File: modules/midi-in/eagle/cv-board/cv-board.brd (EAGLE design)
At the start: 100 x 80 mm, 50 parts, among them IC2 TL072P, IC3 TL074P, IC4 TL074P, T1 BC547, T2 BC547, X1 POWER IN

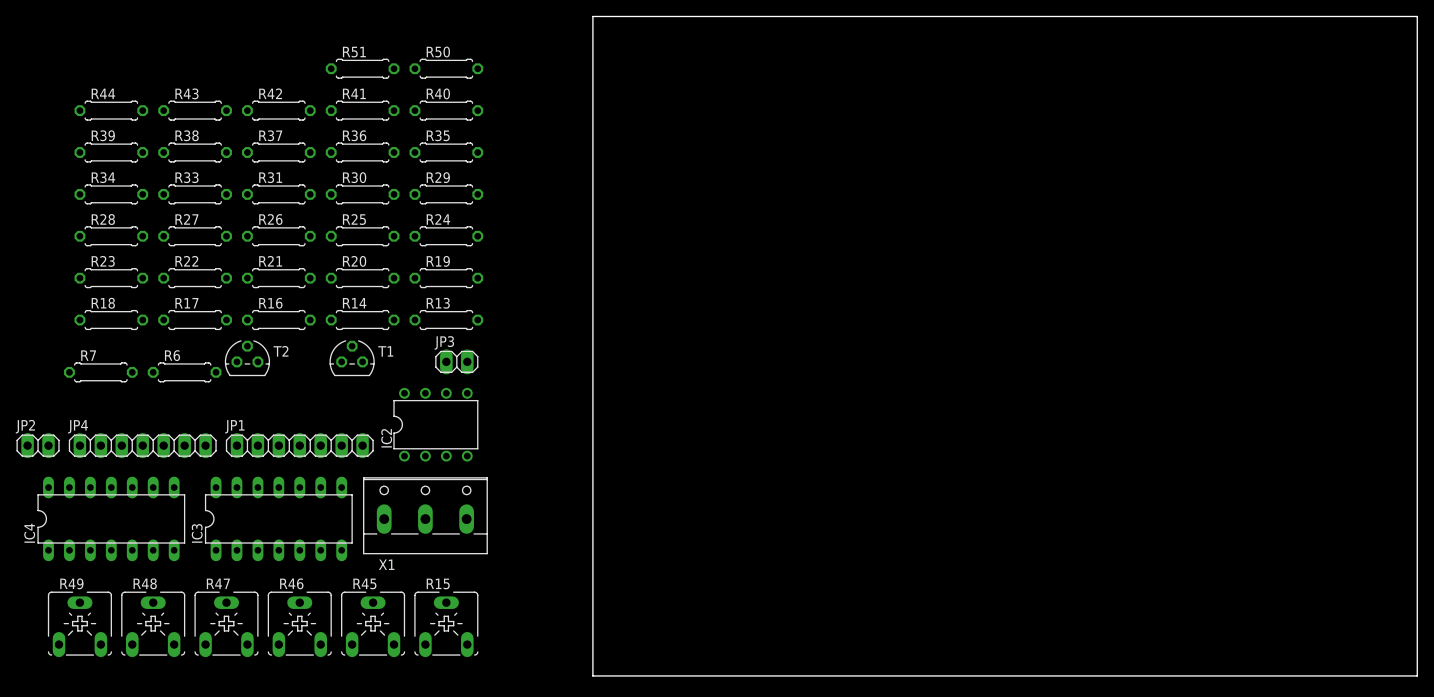
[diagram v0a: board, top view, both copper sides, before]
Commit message: Probably doomed attempt at routing CV board.
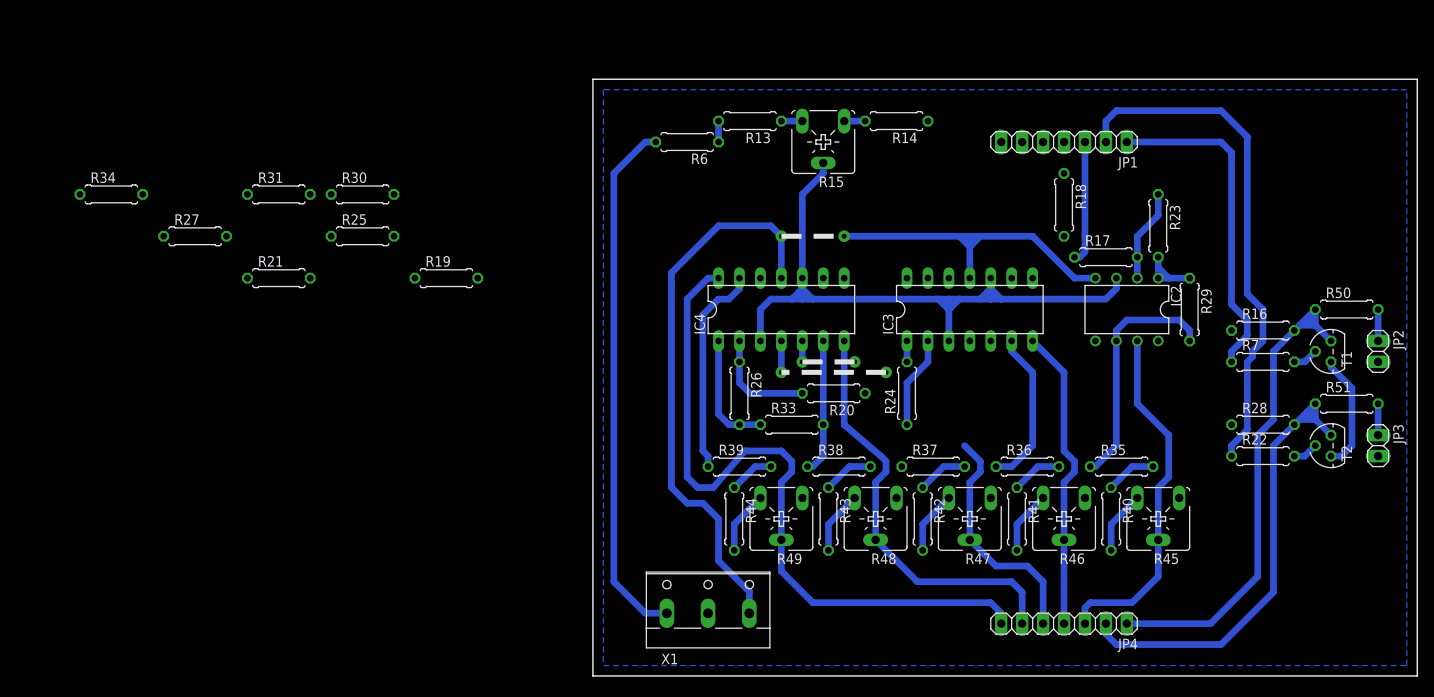
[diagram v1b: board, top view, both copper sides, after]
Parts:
- moved JP2 163.0 mm to (95.2, 39.4), turned to 270 degrees
- moved R28 141.6 mm to (81.3, 30.5)
- moved R7 141.0 mm to (81.3, 38.1)
- moved T2 131.8 mm to (89.5, 27.9), turned to 90 degrees
- moved R22 131.3 mm to (81.3, 26.7)
- moved R23 127.2 mm to (68.6, 54.6), turned to 270 degrees
- moved R51 126.1 mm to (91.4, 33.0)
- moved R16 119.4 mm to (81.3, 41.9)
- moved T1 118.8 mm to (89.5, 39.4), turned to 90 degrees
- moved R18 116.4 mm to (57.1, 57.1), turned to 270 degrees
- moved JP4 113.8 mm to (57.1, 6.35), turned to 180 degrees
- moved R50 113.1 mm to (91.4, 44.5)
- moved JP3 112.2 mm to (95.2, 27.9), turned to 270 degrees
- moved R17 110.8 mm to (62.2, 50.8)
- moved JP1 99.8 mm to (57.1, 64.8), turned to 180 degrees
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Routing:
- net N$41: track 0.00 -> 108.9 mm, vias 0 -> 2
- net N$71: track 0.00 -> 86.2 mm
- net N$8: track 0.00 -> 85.3 mm
- net VCC: track 0.00 -> 82.4 mm
- net N$12: track 0.00 -> 62.6 mm
- net N$20: track 0.00 -> 60.9 mm
- net N$22: track 0.00 -> 57.6 mm
- net N$70: track 0.00 -> 51.2 mm
- net N$67: track 0.00 -> 43.1 mm
- net N$11: track 0.00 -> 40.2 mm
- net N$68: track 0.00 -> 36.9 mm
- net N$34: track 0.00 -> 29.4 mm
- net N$69: track 0.00 -> 28.8 mm
- net N$40: track 0.00 -> 25.7 mm
- net N$36: track 0.00 -> 19.2 mm
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- added copper zone on layer 16, net GND
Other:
- board size 100 x 80 mm -> 100 x 72.4 mm

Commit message: Finish CV board,
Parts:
- moved R30 81.1 mm to (51.4, 41.9), turned to 90 degrees
- moved R31 73.0 mm to (33.0, 41.9), turned to 270 degrees
- moved R34 70.0 mm to (10.2, 44.5), turned to 270 degrees
- moved R19 68.1 mm to (49.5, 58.4), turned to 180 degrees
- moved R25 66.9 mm to (38.7, 58.4), turned to 180 degrees
- moved R27 58.4 mm to (10.2, 54.6), turned to 270 degrees
- moved R21 55.5 mm to (16.5, 58.4), turned to 180 degrees
- moved R20 30.2 mm to (40.6, 62.2)
- moved R18 12.8 mm to (55.9, 44.5)
- moved R33 11.5 mm to (25.1, 41.9), turned to 90 degrees
- moved R23 10.9 mm to (77.5, 61.0), turned to 0 degrees
- moved R24 10.9 mm to (48.6, 31.4), turned to 180 degrees
- moved R29 10.2 mm to (77.5, 53.3)
- moved R17 9.67 mm to (66.0, 59.7)
- moved IC4 6.48 mm to (16.5, 45.7), turned to 90 degrees
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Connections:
- net VCC renamed N$30
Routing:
- net N$30: track 82.4 -> 138.9 mm, vias 0 -> 19
- net GND: track 2.54 -> 41.7 mm, vias 1 -> 10
- net N$18: track 0.00 -> 31.8 mm
- net N$37: track 0.00 -> 30.0 mm
- net N$3: track 13.2 -> 42.5 mm, vias 0 -> 1
- net N$38: track 0.00 -> 26.2 mm
- net N$69: track 28.8 -> 54.4 mm
- net N$71: track 86.2 -> 65.5 mm
- net N$15: track 0.00 -> 17.0 mm
- net N$33: track 8.15 -> 23.8 mm
- net N$11: track 40.2 -> 55.4 mm
- net N$27: track 11.2 -> 26.0 mm
- net N$29: track 0.00 -> 14.7 mm
- net N$70: track 51.2 -> 65.0 mm
- net N$32: track 0.00 -> 13.8 mm
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- added copper zone on layer 16, net N$14
- added copper zone on layer 16, net N$25
- added copper zone on layer 16, net N$31
- added copper zone on layer 16, net N$43
- added copper zone on layer 16, net N$46
- added copper zone on layer 16, net N$47
- added copper zone on layer 16, net N$48
- added copper zone on layer 16, net N$49
- added copper zone on layer 16, net N$6
- added copper zone on layer 16, net N$9
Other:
- board text added: "MARCH 2016"
- board text added: "MICHD"
